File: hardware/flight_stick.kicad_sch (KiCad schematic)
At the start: 25 parts, among them J10 USB_C_Receptacle_USB2.0, J2 Conn_02x05_Top_Bottom, J9 Conn_ST_STDC14, SW1 KMR223G LFG, U2 AT24CS01-MAHM, U4 STM32F103CBU6, U5 USBLC6-2SC6, Y1 8M

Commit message: Completed first layout draft
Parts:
- removed J2: Conn_02x05_Top_Bottom, Connector_JST:JST_J2100_B10B-J21DK-GGXR_2x05_P2.50x4.00mm_Vertical, symbol Connector_Generic:Conn_02x05_Top_Bottom
- added J2: Conn_02x05_Odd_Even, Connector_JST:JST_PUD_B10B-PUDSS_2x05_P2.00mm_Vertical, symbol Connector_Generic:Conn_02x05_Odd_Even
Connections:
- net ADC_CS: now also U4.30 (PA9); no longer U4.21 (PB10)
- net ADC_RST: now also U4.31 (PA10); no longer U4.22 (PB11)
- net COMPRT_RX: now also U4.43 (PB7); no longer U4.31 (PA10)
- net COMPRT_TX: now also U4.42 (PB6); no longer U4.30 (PA9)
- net EEPROM_SCK: now also U4.21 (PB10); no longer U4.42 (PB6)
- net EEPROM_SDA: now also U4.22 (PB11); no longer U4.43 (PB7)
- net MTX_COL1: now also U4.15 (PA5), J2.2 (Pin_2); no longer U4.11 (PA1)
- net MTX_COL2: now also U4.14 (PA4), J2.4 (Pin_4); no longer U4.12 (PA2)
- net MTX_COL3: now also J2.6 (Pin_6)
- net MTX_COL4: now also U4.12 (PA2), J2.8 (Pin_8); no longer U4.14 (PA4)
- net MTX_COL5: now also U4.11 (PA1), J2.10 (Pin_10); no longer U4.15 (PA5)
- net MTX_ROW1: now also J2.1 (Pin_1)
- net MTX_ROW2: now also J2.3 (Pin_3)
- net MTX_ROW3: now also J2.5 (Pin_5)
- net MTX_ROW4: now also J2.7 (Pin_7)
- net MTX_ROW5: now also J2.9 (Pin_9)
- net OSC+: now reaches U4.5 (PD0), Y1.1
- net OSC-: now reaches U4.6 (PD1), Y1.3

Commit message: resolved comments
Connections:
- net D+: no longer R7.2
- net USBP: now also R7.2
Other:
- sheet Power renamed CAN Power
- note removed: "NOTE: ALL GPIO pins will be routed and selected AFTER inital layout is complete with Essential routing"
- moved on the sheet: J2, R7, U5

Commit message: Resolved comments
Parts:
- removed H1, H2, H3: MountingHole, MountingHole:MountingHole_3.2mm_M3, symbol Mechanical:MountingHole
- J2: footprint Connector_JST:JST_PUD_B10B-PUDSS_2x05_P2.00mm_Vertical -> Connector_JST:JST_PHD_B10B-PHDSS_2x05_P2.00mm_Vertical; LCSC (none) -> C471519
- R10, R8: LCSC C849792 -> C114664
- R2, R3: LCSC C23345 -> C99782
- R7: LCSC C23345 -> C22843
- R9: LCSC C105588 -> C114664
- U2: LCSC (none) -> C616851
- U5: LCSC (none) -> C7519
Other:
- sheet CAN Power renamed Power
- moved on the sheet: C16, C17, C18, C19, R20, SW1, U4, Y1

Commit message: updated comments
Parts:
- J2: LCSC C471519 -> C158039
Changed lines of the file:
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@@
 			)
 		)
-		(property "LCSC" "C471519"
+		(property "LCSC" "C158039"
 			(at 187.96 97.79 0)
 			(effects

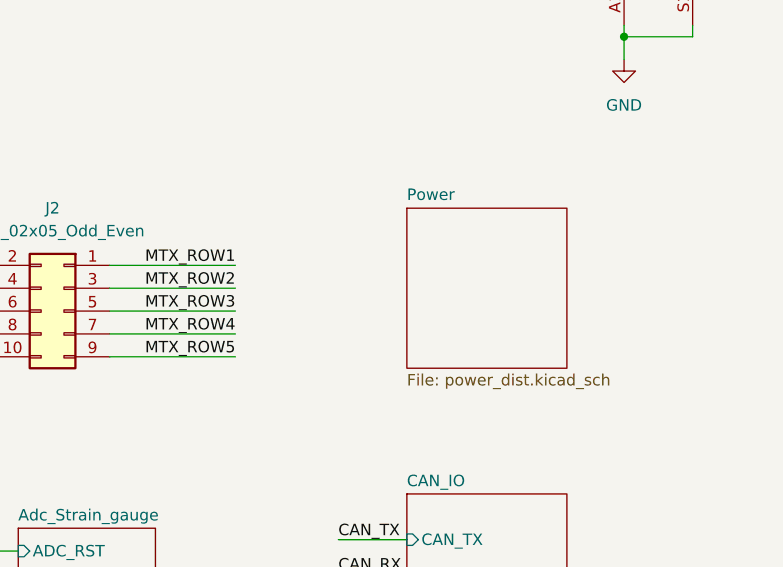
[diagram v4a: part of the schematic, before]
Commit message: tied PG to mcu reset
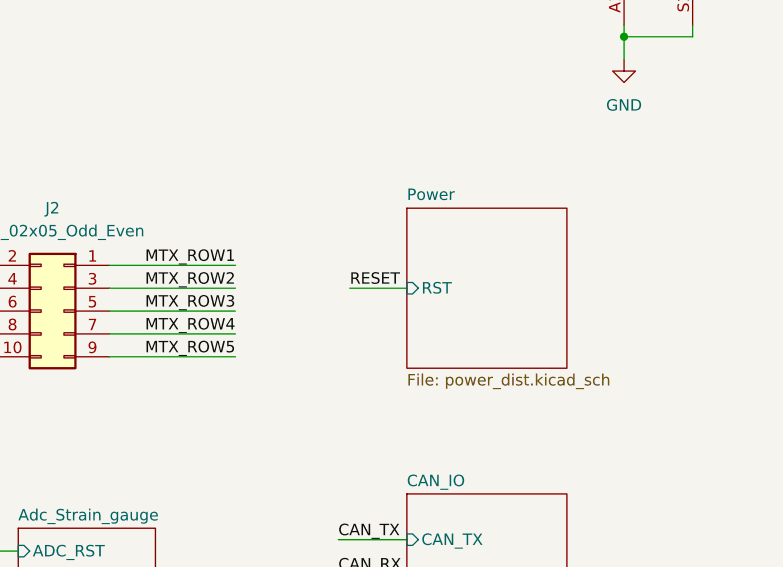
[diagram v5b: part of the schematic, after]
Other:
- sheet Power ports: added RST; removed none
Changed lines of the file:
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@@
 	(wire
 		(pts
+			(xy 219.71 95.25) (xy 226.06 95.25)
+		)
+		(stroke
+			(width 0)
+			(type default)
+		)
+	)
+	(wire
+		(pts
 			(xy 36.83 157.48) (xy 72.39 157.48)
 		)
@@
 		)
 	)
+	(label "RESET"
+		(at 219.71 95.25 0)
+		(effects
+			(font
+				(size 1.27 1.27)
+			)
+			(justify left bottom)
+		)
+	)
 	(label "MTX_ROW3"
 		(at 207.01 97.79 180)
@@
 			)
 		)
+		(pin "RST" input
+			(at 226.06 95.25 180)
+			(effects
+				(font
+					(size 1.27 1.27)
+				)
+				(justify left)
+			)
+		)

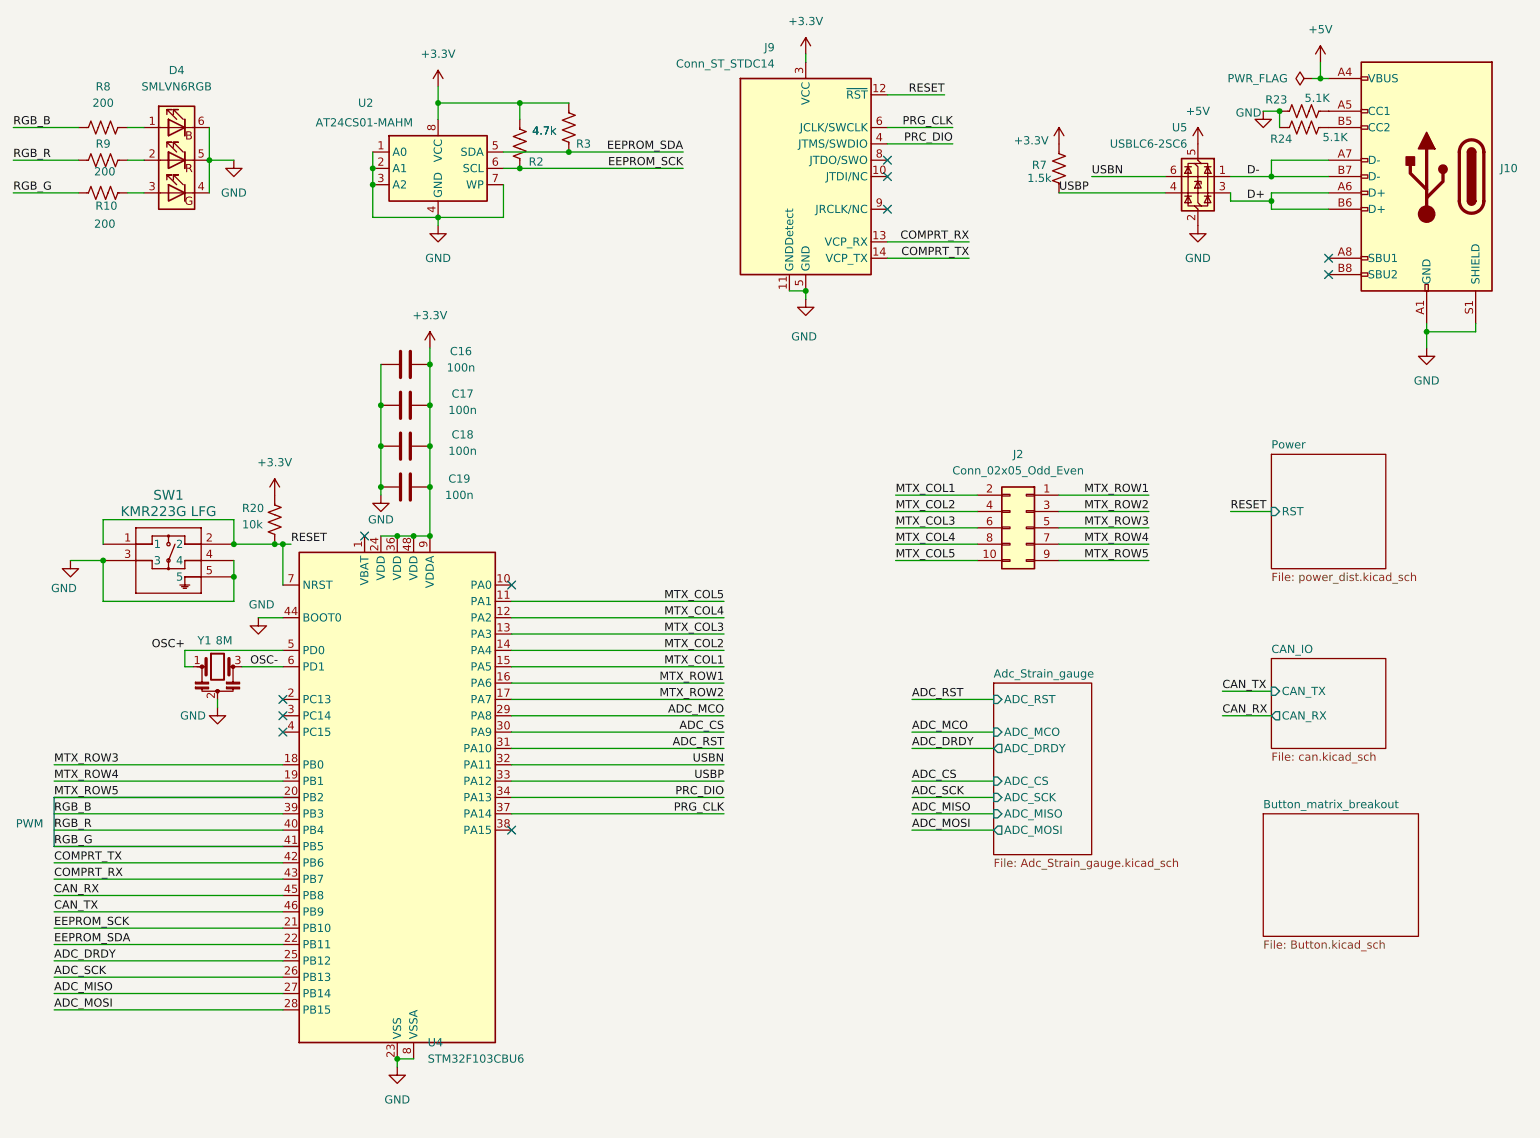
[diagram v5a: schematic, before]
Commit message: Refactor netlist and lock footprints in PCB design
Renamed the /RESET net to /~{RESET} and updated all references accordingly. Reordered and renumbered net definitions to maintain consistency. Added the 'locked' attribute to multiple footprints for improved layout stability. Updated silkscreen reference positions for R8 and R10. No functional changes to the schematic or board layout.
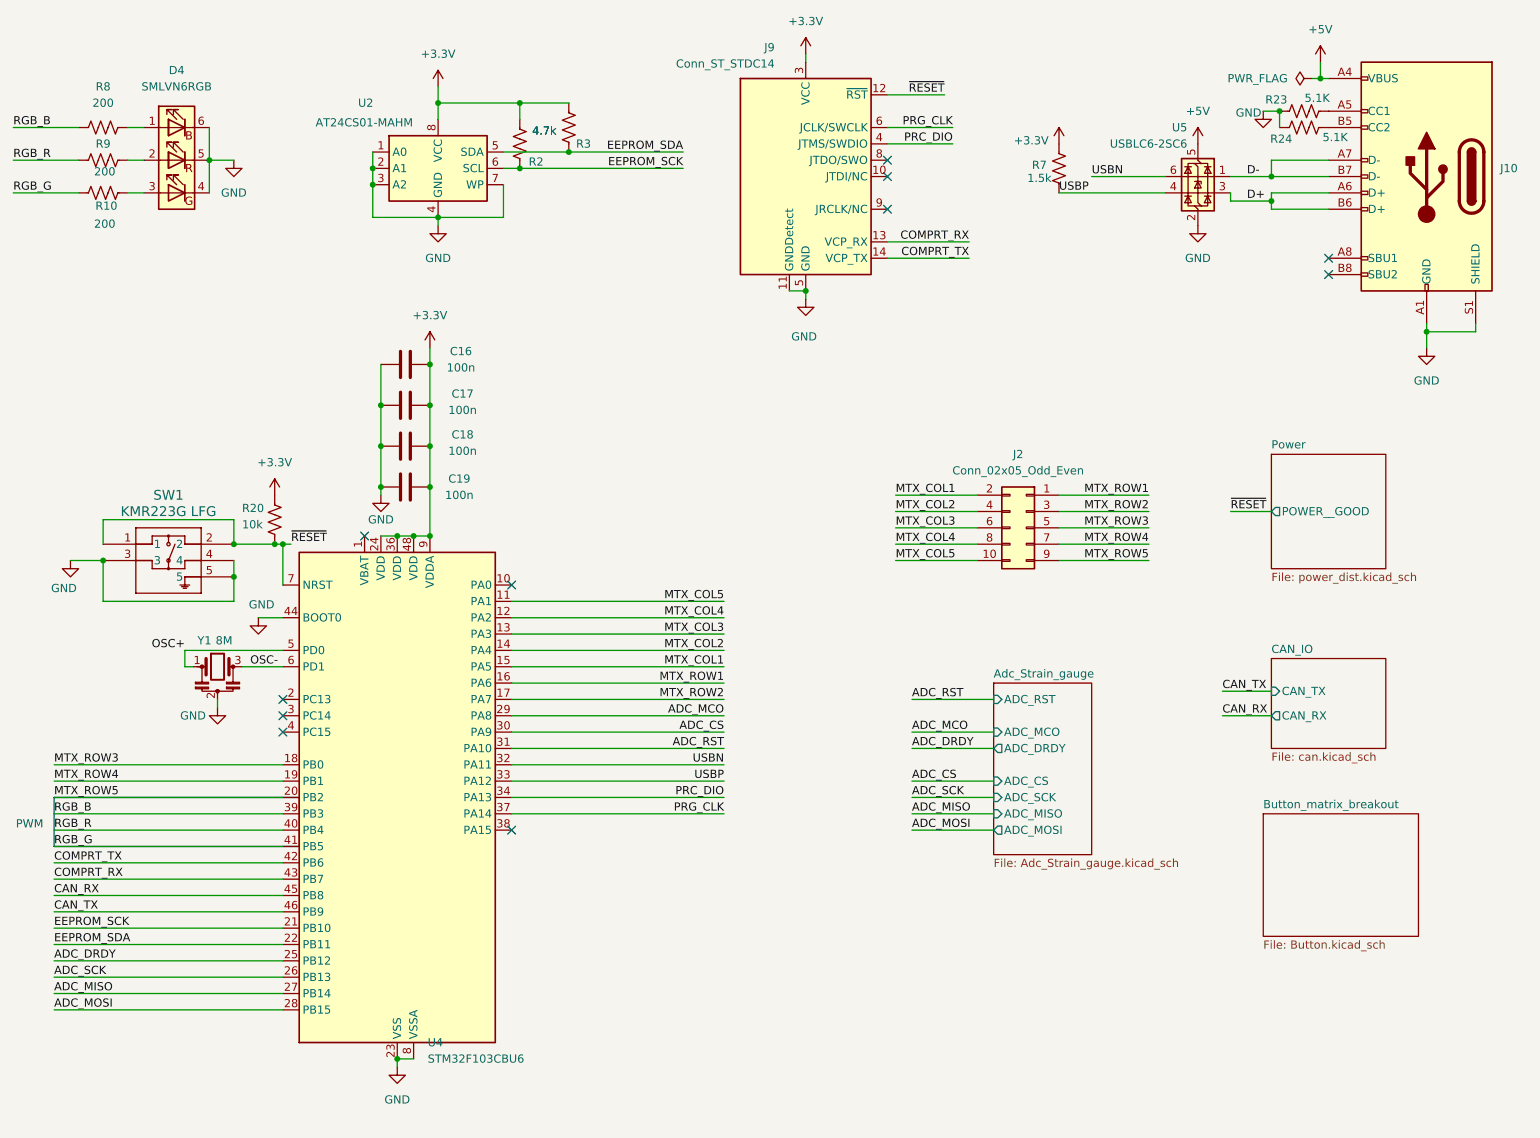
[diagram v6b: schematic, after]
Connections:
- net RESET renamed ~{RESET}
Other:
- sheet Power ports: added POWER__GOOD; removed RST
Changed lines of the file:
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@@
 		)
 	)
-	(label "RESET"
-		(at 175.26 30.48 180)
+	(label "RGB_G"
+		(at 36.83 147.32 0)
 		(effects
 			(font
 				(size 1.27 1.27)
 			)
-			(justify right bottom)
+			(justify left bottom)
 		)
 	)
-	(label "RGB_G"
-		(at 36.83 147.32 0)
+	(label "~{RESET}"
+		(at 175.26 30.48 180)
 		(effects
 			(font
 				(size 1.27 1.27)
 			)
-			(justify left bottom)
+			(justify right bottom)
 		)
 	)
@@
 		)
 	)
+	(label "~{RESET}"
+		(at 219.71 95.25 0)
+		(effects
+			(font
+				(size 1.27 1.27)
+			)
+			(justify left bottom)
+		)
+	)
 	(label "COMPRT_TX"
 		(at 36.83 149.86 0)
@@
 		)
 	)
-	(label "RESET"
-		(at 219.71 95.25 0)
-		(effects
-			(font
-				(size 1.27 1.27)
-			)
-			(justify left bottom)
-		)
-	)
 	(label "MTX_ROW3"
 		(at 207.01 97.79 180)
@@
 		)
 	)
-	(label "RESET"
+	(label "~{RESET}"
 		(at 73.66 100.33 0)
 		(effects
@@
 			)
 		)
-		(pin "RST" input
+		(pin "POWER__GOOD" output
 			(at 226.06 95.25 180)
 			(effects
